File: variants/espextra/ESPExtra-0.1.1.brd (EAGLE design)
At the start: 95.6 x 57.1 mm, 12 parts, among them U1 ESP12E_DEVKIT, U2 MCP23S17SP, U3 MCP23S17SP, U4 MCP3008

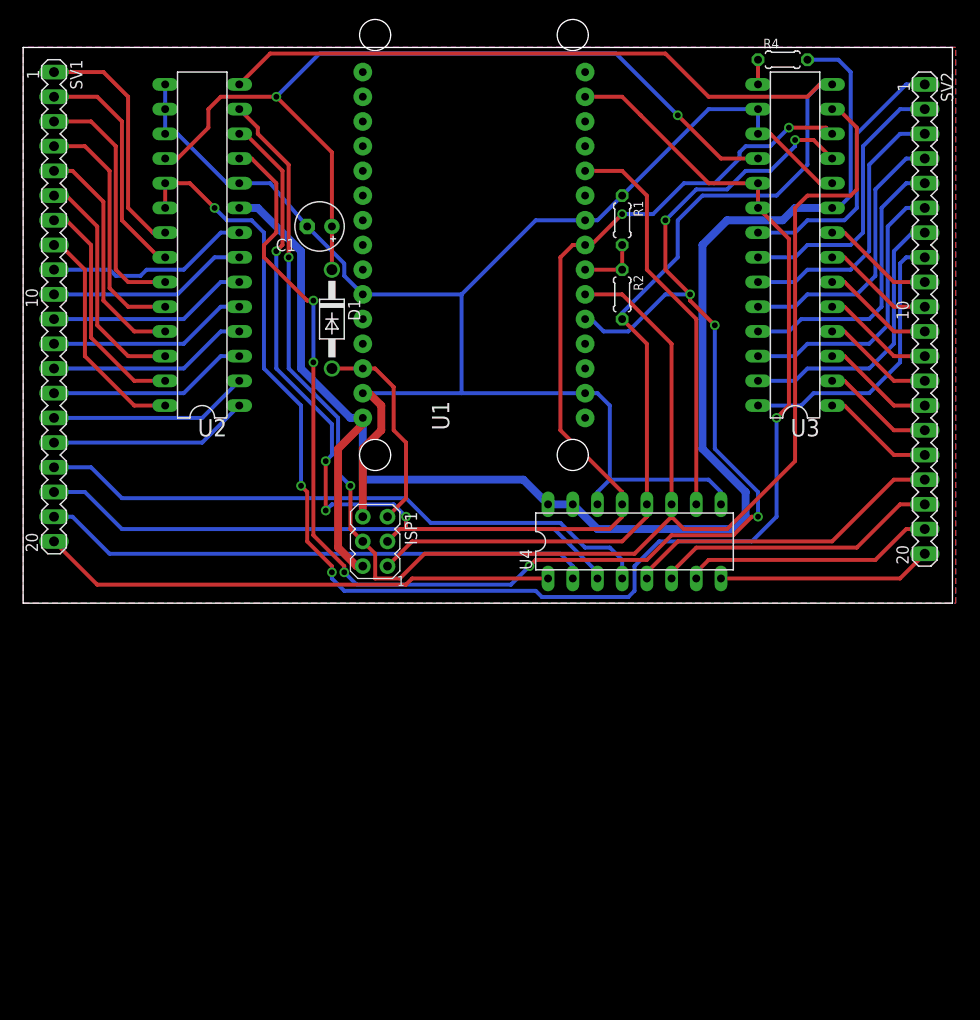
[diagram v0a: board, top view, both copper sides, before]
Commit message: Updated the board schematic to use 3V3. Using 5V is not working.
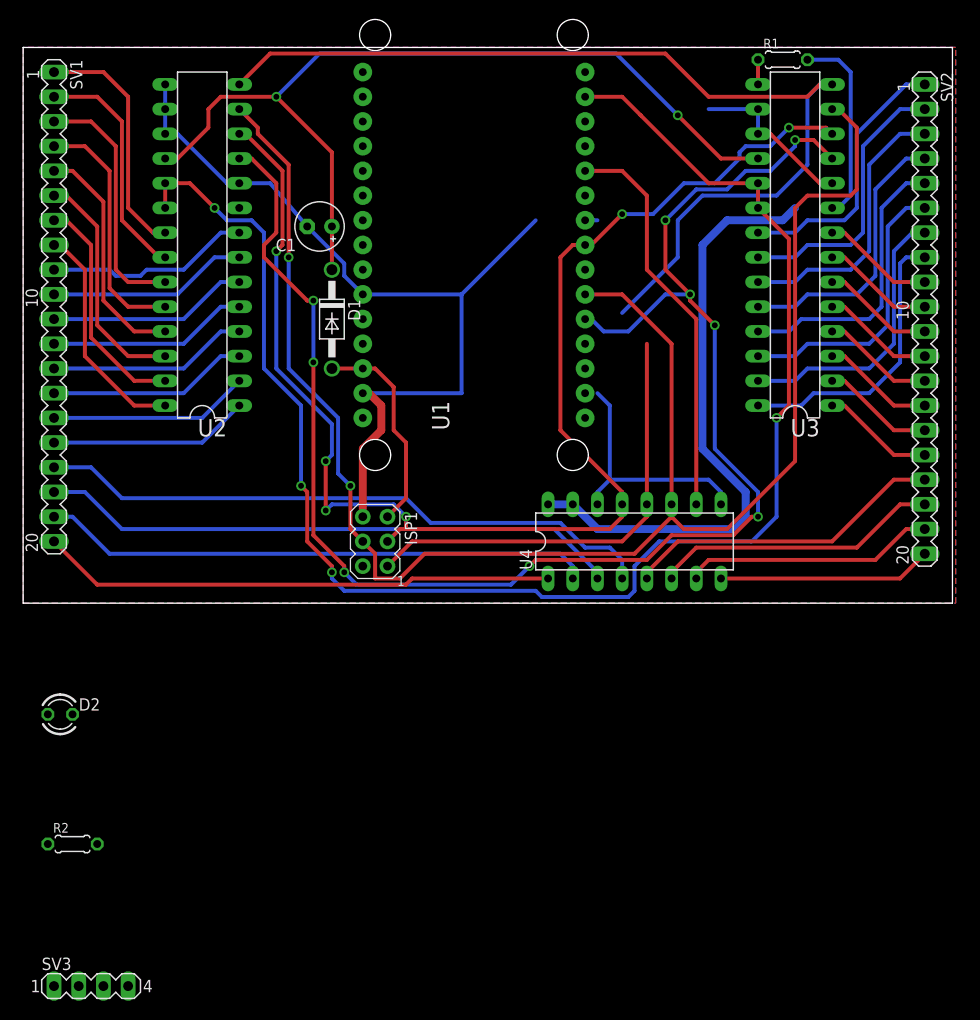
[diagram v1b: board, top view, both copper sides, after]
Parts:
- removed R4: 4k7, resistor:0204/5
- added D2: (no value), led:LED3MM
- added SV3: (no value), con-lstb:MA04-1
- R1: value 910 -> 10k
- R2: value 470 -> 100
- moved R2 79.9 mm to (5.08, -24.8), turned to 0 degrees
- moved R1 23.3 mm to (78.1, 55.9), turned to 0 degrees
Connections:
- removed net +5V: ISP1.2, R4.2, U1.VIN, U2.9, U3.9, U4.15, U4.16
- removed net N$11: R1.2, R2.1, U1.D6
- new net +3V3: ISP1.2, R1.2, U1.3V3@0, U1.3V3@1, U1.3V3@2, U2.9, U3.9, U4.15, U4.16
- new net CS_0: SV3.2, U1.D2
- new net CS_1: SV3.3, U1.D3
- new net CS_2: SV3.4, U1.D0
- new net N$1: D2.A, R2.1
- net A0: now also SV3.1
- net D0: now also R2.2
- net GND: now also D2.K; no longer R1.1
- net MISO: now also U1.D6; no longer R2.2
- net N$25: now also R1.1; no longer R4.1
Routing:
- net +5V: track 160.2 -> 0.00 mm
- net +3V3: track 0.00 -> 82.9 mm
- net GND: track 168.6 -> 133.4 mm
- net N$11: track 6.35 -> 0.00 mm
- net MISO: track 153.1 -> 148.8 mm
